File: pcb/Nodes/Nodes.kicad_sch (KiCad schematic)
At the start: 7 parts, among them J1 Conn_Coaxial, J2 Conn_01x04_Pin, U1 XIAO-RP2040-DIP, U2 RFM9X, U3 TLV73333PDBVR

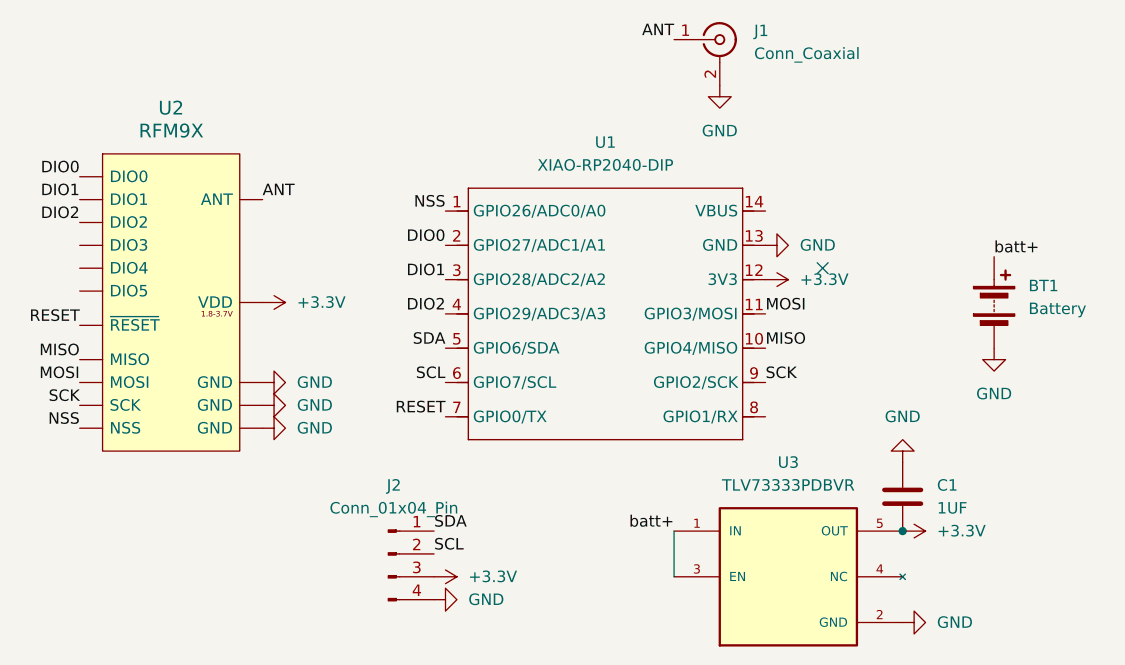
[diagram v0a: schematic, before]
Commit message: Node work + GNSS concept
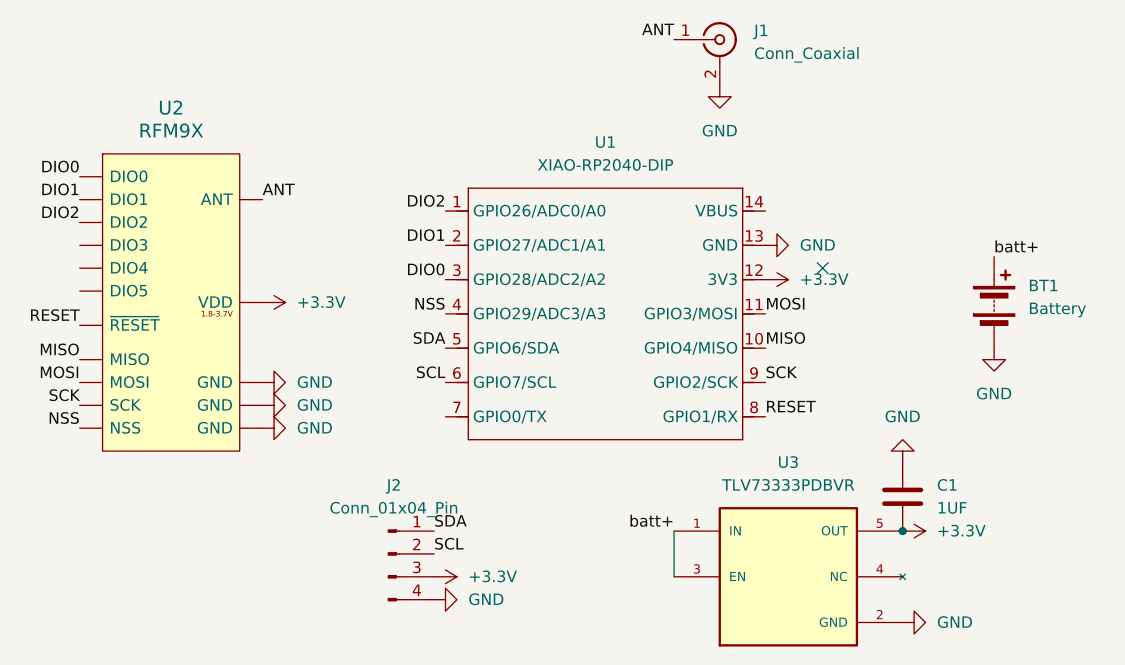
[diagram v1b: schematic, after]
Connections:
- net DIO0: now also U1.3 (GPIO28/ADC2/A2); no longer U1.2 (GPIO27/ADC1/A1)
- net DIO1: now also U1.2 (GPIO27/ADC1/A1); no longer U1.3 (GPIO28/ADC2/A2)
- net DIO2: now also U1.1 (GPIO26/ADC0/A0); no longer U1.4 (GPIO29/ADC3/A3)
- net NSS: now also U1.4 (GPIO29/ADC3/A3); no longer U1.1 (GPIO26/ADC0/A0)
- net RESET: now also U1.8 (GPIO1/RX); no longer U1.7 (GPIO0/TX)
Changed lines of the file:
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@@
 	)
 	(label "DIO2"
-		(at 130.81 67.31 180)
+		(at 130.81 55.88 180)
 		(effects
 			(font
@@
 	)
 	(label "DIO0"
-		(at 130.81 59.69 180)
+		(at 130.81 63.5 180)
 		(effects
 			(font
@@
 	)
 	(label "NSS"
-		(at 130.81 55.88 180)
+		(at 130.81 67.31 180)
 		(effects
 			(font
@@
 	)
 	(label "RESET"
-		(at 130.81 78.74 180)
+		(at 166.37 78.74 0)
 		(effects
 			(font
 				(size 1.27 1.27)
 			)
-			(justify right bottom)
+			(justify left bottom)
 		)
 	)
@@
 	)
 	(label "DIO1"
-		(at 130.81 63.5 180)
+		(at 130.81 59.69 180)
 		(effects
 			(font
